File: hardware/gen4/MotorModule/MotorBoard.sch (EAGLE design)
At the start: 65 parts, among them IC1 XMEGA16A4A, M1O1 TEST_PT, M1O2 TEST_PT, M1O3 TEST_PT

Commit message: changes to motor and main board
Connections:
- net 12V: now also JP3.5, JP3.6
- net 12VGND: now also JP3.35, JP3.36
- net GND: now also JP3.33; no longer JP3.36
- net N$3: now also JP3.27; no longer JP3.31
- net N$34: now also JP3.31; no longer JP3.35
- net N$4: now also JP3.29; no longer JP3.33
- net N$45: now also JP3.25; no longer JP3.29
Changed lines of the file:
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@@
 <instance part="S2" gate="S" x="12.7" y="182.88"/>
 <instance part="GND10" gate="1" x="215.9" y="55.88" rot="R270"/>
-<instance part="GND14" gate="1" x="256.54" y="35.56"/>
+<instance part="GND14" gate="1" x="254" y="35.56"/>
 <instance part="U$1" gate="G$1" x="86.36" y="86.36" rot="R270"/>
 <instance part="C3" gate="G$1" x="111.76" y="132.08" rot="R180"/>
@@
 <pinref part="U$5" gate="G$1" pin="GND"/>
 <wire x1="215.9" y1="152.4" x2="215.9" y2="149.86" width="0.1524" layer="91"/>
-<label x="243.84" y="30.48" size="1.778" layer="95"/>
+<label x="243.84" y="33.02" size="1.778" layer="95"/>
 <pinref part="GND5" gate="1" pin="GND"/>
 </segment>
@@
 <segment>
 <pinref part="GND14" gate="1" pin="GND"/>
-<wire x1="256.54" y1="38.1" x2="241.3" y2="38.1" width="0.1524" layer="91"/>
+<wire x1="254" y1="38.1" x2="241.3" y2="38.1" width="0.1524" layer="91"/>
 <pinref part="JP3" gate="G$1" pin="30"/>
 <junction x="241.3" y="38.1"/>
@@
 </segment>
 <segment>
-<wire x1="241.3" y1="30.48" x2="243.84" y2="30.48" width="0.1524" layer="91"/>
-<wire x1="241.3" y1="30.48" x2="241.3" y2="33.02" width="0.1524" layer="91"/>
 <pinref part="JP3" gate="G$1" pin="34"/>
-<pinref part="JP3" gate="G$1" pin="36"/>
-<junction x="241.3" y="30.48"/>
+<wire x1="243.84" y1="33.02" x2="241.3" y2="33.02" width="0.1524" layer="91"/>
+<pinref part="JP3" gate="G$1" pin="33"/>
+<wire x1="241.3" y1="33.02" x2="226.06" y2="33.02" width="0.1524" layer="91"/>
 </segment>
 <segment>
@@
 <pinref part="R3" gate="G$1" pin="2"/>
 <wire x1="213.36" y1="20.32" x2="215.9" y2="20.32" width="0.1524" layer="91"/>
-<wire x1="215.9" y1="20.32" x2="215.9" y2="27.94" width="0.1524" layer="91"/>
-<wire x1="215.9" y1="27.94" x2="223.52" y2="35.56" width="0.1524" layer="91"/>
-<wire x1="223.52" y1="35.56" x2="226.06" y2="35.56" width="0.1524" layer="91"/>
-<pinref part="JP3" gate="G$1" pin="31"/>
+<wire x1="215.9" y1="20.32" x2="215.9" y2="30.48" width="0.1524" layer="91"/>
+<pinref part="JP3" gate="G$1" pin="27"/>
+<wire x1="215.9" y1="30.48" x2="226.06" y2="40.64" width="0.1524" layer="91"/>
 </segment>
 </net>
@@
 <segment>
 <pinref part="R4" gate="G$1" pin="2"/>
-<wire x1="218.44" y1="15.24" x2="218.44" y2="27.94" width="0.1524" layer="91"/>
-<wire x1="218.44" y1="27.94" x2="223.52" y2="33.02" width="0.1524" layer="91"/>
-<wire x1="223.52" y1="33.02" x2="226.06" y2="33.02" width="0.1524" layer="91"/>
-<pinref part="JP3" gate="G$1" pin="33"/>
+<wire x1="218.44" y1="15.24" x2="218.44" y2="30.48" width="0.1524" layer="91"/>
+<pinref part="JP3" gate="G$1" pin="29"/>
+<wire x1="226.06" y1="38.1" x2="218.44" y2="30.48" width="0.1524" layer="91"/>
 </segment>
 </net>
@@
 <junction x="226.06" y="73.66"/>
 <pinref part="JP3" gate="G$1" pin="3"/>
+<pinref part="JP3" gate="G$1" pin="5"/>
+<wire x1="226.06" y1="71.12" x2="226.06" y2="68.58" width="0.1524" layer="91"/>
+<pinref part="JP3" gate="G$1" pin="6"/>
+<wire x1="241.3" y1="71.12" x2="241.3" y2="68.58" width="0.1524" layer="91"/>
+<junction x="241.3" y="71.12"/>
+<junction x="226.06" y="71.12"/>
+<junction x="226.06" y="68.58"/>
+<junction x="241.3" y="68.58"/>
 </segment>
 <segment>
@@
 <wire x1="241.3" y1="25.4" x2="241.3" y2="27.94" width="0.1524" layer="91"/>
 <junction x="241.3" y="25.4"/>
+<pinref part="JP3" gate="G$1" pin="35"/>
+<wire x1="226.06" y1="27.94" x2="226.06" y2="30.48" width="0.1524" layer="91"/>
+<pinref part="JP3" gate="G$1" pin="36"/>
+<wire x1="241.3" y1="27.94" x2="241.3" y2="30.48" width="0.1524" layer="91"/>
+<junction x="226.06" y="27.94"/>
+<junction x="226.06" y="30.48"/>
+<junction x="241.3" y="30.48"/>
+<junction x="241.3" y="27.94"/>
 </segment>
 <segment>
@@
 <segment>
 <pinref part="R2" gate="G$1" pin="2"/>
-<wire x1="213.36" y1="25.4" x2="213.36" y2="27.94" width="0.1524" layer="91"/>
-<wire x1="213.36" y1="27.94" x2="223.52" y2="38.1" width="0.1524" layer="91"/>
-<wire x1="223.52" y1="38.1" x2="226.06" y2="38.1" width="0.1524" layer="91"/>
-<pinref part="JP3" gate="G$1" pin="29"/>
+<pinref part="JP3" gate="G$1" pin="25"/>
+<wire x1="226.06" y1="43.18" x2="213.36" y2="30.48" width="0.1524" layer="91"/>
+<wire x1="213.36" y1="30.48" x2="213.36" y2="25.4" width="0.1524" layer="91"/>
 </segment>
 </net>
@@
 <segment>
 <pinref part="R15" gate="G$1" pin="2"/>
-<wire x1="223.52" y1="10.16" x2="223.52" y2="30.48" width="0.1524" layer="91"/>
-<wire x1="223.52" y1="30.48" x2="226.06" y2="30.48" width="0.1524" layer="91"/>
-<pinref part="JP3" gate="G$1" pin="35"/>
-</segment>
-</net>
+<wire x1="223.52" y1="10.16" x2="223.52" y2="33.02" width="0.1524" layer="91"/>
+<pinref part="JP3" gate="G$1" pin="31"/>
+<wire x1="223.52" y1="33.02" x2="226.06" y2="35.56" width="0.1524" layer="91"/>
+</segment>
+</net>

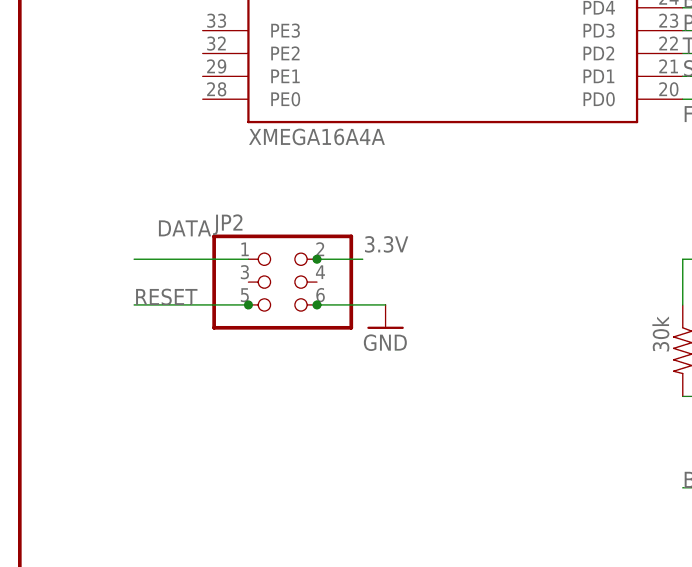
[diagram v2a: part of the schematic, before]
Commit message: motor board push button fix
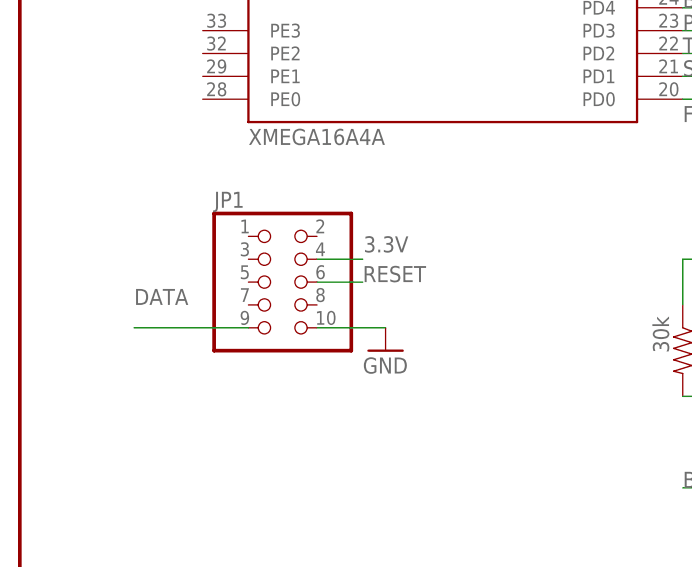
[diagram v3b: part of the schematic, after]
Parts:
- removed JP2: (no value), pinhead:PINHD-2X3
- added JP1: (no value), pinhead:PINHD-2X5
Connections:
- net 3.3V: now also JP1.4; no longer JP2.2
- net DATA: now also JP1.9; no longer JP2.1
- net GND: now also JP1.10; no longer JP2.6
- net RESET: now also JP1.6; no longer JP2.5
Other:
- note removed: "RESET"
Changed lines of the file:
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@@
 <part name="GND15" library="SparkFun-Aesthetics" deviceset="GND" device=""/>
 <part name="GND16" library="SparkFun-Aesthetics" deviceset="GND" device=""/>
-<part name="JP2" library="pinhead" deviceset="PINHD-2X3" device=""/>
 <part name="R18" library="resistor" deviceset="R-US_" device="R2512" value="0.05"/>
+<part name="JP1" library="pinhead" deviceset="PINHD-2X5" device=""/>
 </parts>
 <sheets>
@@
 <text x="73.66" y="88.9" size="1.778" layer="95">FAULTN
 </text>
-<text x="12.7" y="68.58" size="1.778" layer="95">RESET</text>
 <text x="78.74" y="25.4" size="1.778" layer="95">ENABLE</text>
 <text x="73.66" y="106.68" size="1.778" layer="95">ENABLE</text>
@@
 <instance part="R11" gate="G$1" x="91.44" y="25.4" rot="R180"/>
 <instance part="R15" gate="G$1" x="218.44" y="10.16"/>
-<instance part="GND1" gate="1" x="40.64" y="66.04"/>
+<instance part="GND1" gate="1" x="40.64" y="63.5"/>
 <instance part="IC2" gate="G$1" x="127" y="132.08"/>
 <instance part="GND4" gate="1" x="127" y="124.46"/>
@@
 <instance part="GND15" gate="1" x="111.76" y="124.46"/>
 <instance part="GND16" gate="1" x="142.24" y="124.46"/>
-<instance part="JP2" gate="A" x="27.94" y="71.12"/>
 <instance part="R18" gate="G$1" x="149.86" y="7.62" rot="R90"/>
+<instance part="JP1" gate="A" x="27.94" y="71.12"/>
 </instances>
 <busses>
@@
 </segment>
 <segment>
-<wire x1="33.02" y1="68.58" x2="40.64" y2="68.58" width="0.1524" layer="91"/>
+<wire x1="33.02" y1="66.04" x2="40.64" y2="66.04" width="0.1524" layer="91"/>
 <pinref part="GND1" gate="1" pin="GND"/>
-<pinref part="JP2" gate="A" pin="6"/>
-<junction x="33.02" y="68.58"/>
+<pinref part="JP1" gate="A" pin="10"/>
 </segment>
 <segment>
@@
 </segment>
 <segment>
-<wire x1="12.7" y1="68.58" x2="25.4" y2="68.58" width="0.1524" layer="91"/>
-<pinref part="JP2" gate="A" pin="5"/>
-<junction x="25.4" y="68.58"/>
+<wire x1="33.02" y1="71.12" x2="38.1" y2="71.12" width="0.1524" layer="91"/>
+<label x="38.1" y="71.12" size="1.778" layer="95"/>
+<pinref part="JP1" gate="A" pin="6"/>
 </segment>
 </net>
@@
 <segment>
 <wire x1="33.02" y1="73.66" x2="38.1" y2="73.66" width="0.1524" layer="91"/>
-<pinref part="JP2" gate="A" pin="2"/>
-<junction x="33.02" y="73.66"/>
+<pinref part="JP1" gate="A" pin="4"/>
 </segment>
 <segment>
@@
 </segment>
 <segment>
-<pinref part="JP2" gate="A" pin="1"/>
-<wire x1="25.4" y1="73.66" x2="12.7" y2="73.66" width="0.1524" layer="91"/>
-<label x="15.24" y="76.2" size="1.778" layer="95"/>
-</segment>
-</net>
+<wire x1="25.4" y1="66.04" x2="12.7" y2="66.04" width="0.1524" layer="91"/>
+<label x="12.7" y="68.58" size="1.778" layer="95"/>
+<pinref part="JP1" gate="A" pin="9"/>
+</segment>
+</net>

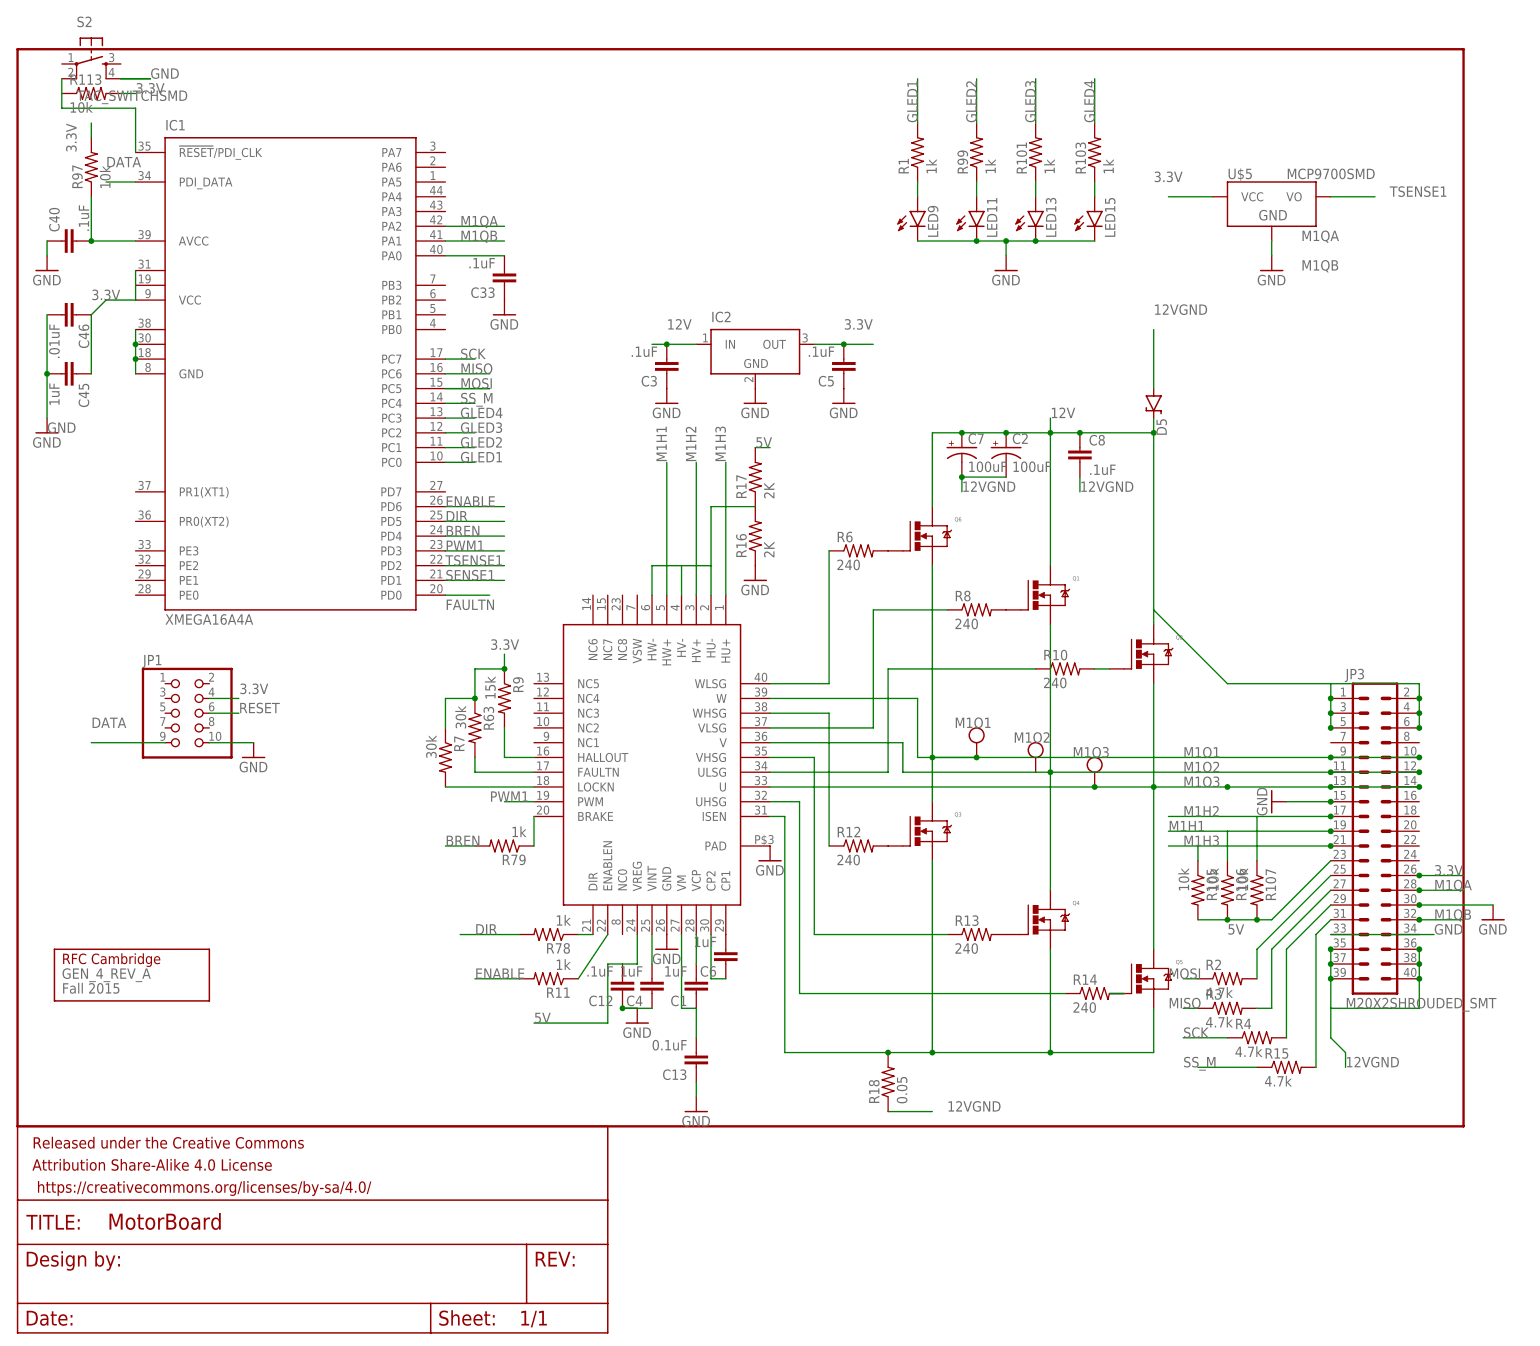
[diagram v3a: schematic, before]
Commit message: fixed ten thousand net issues on motorboard
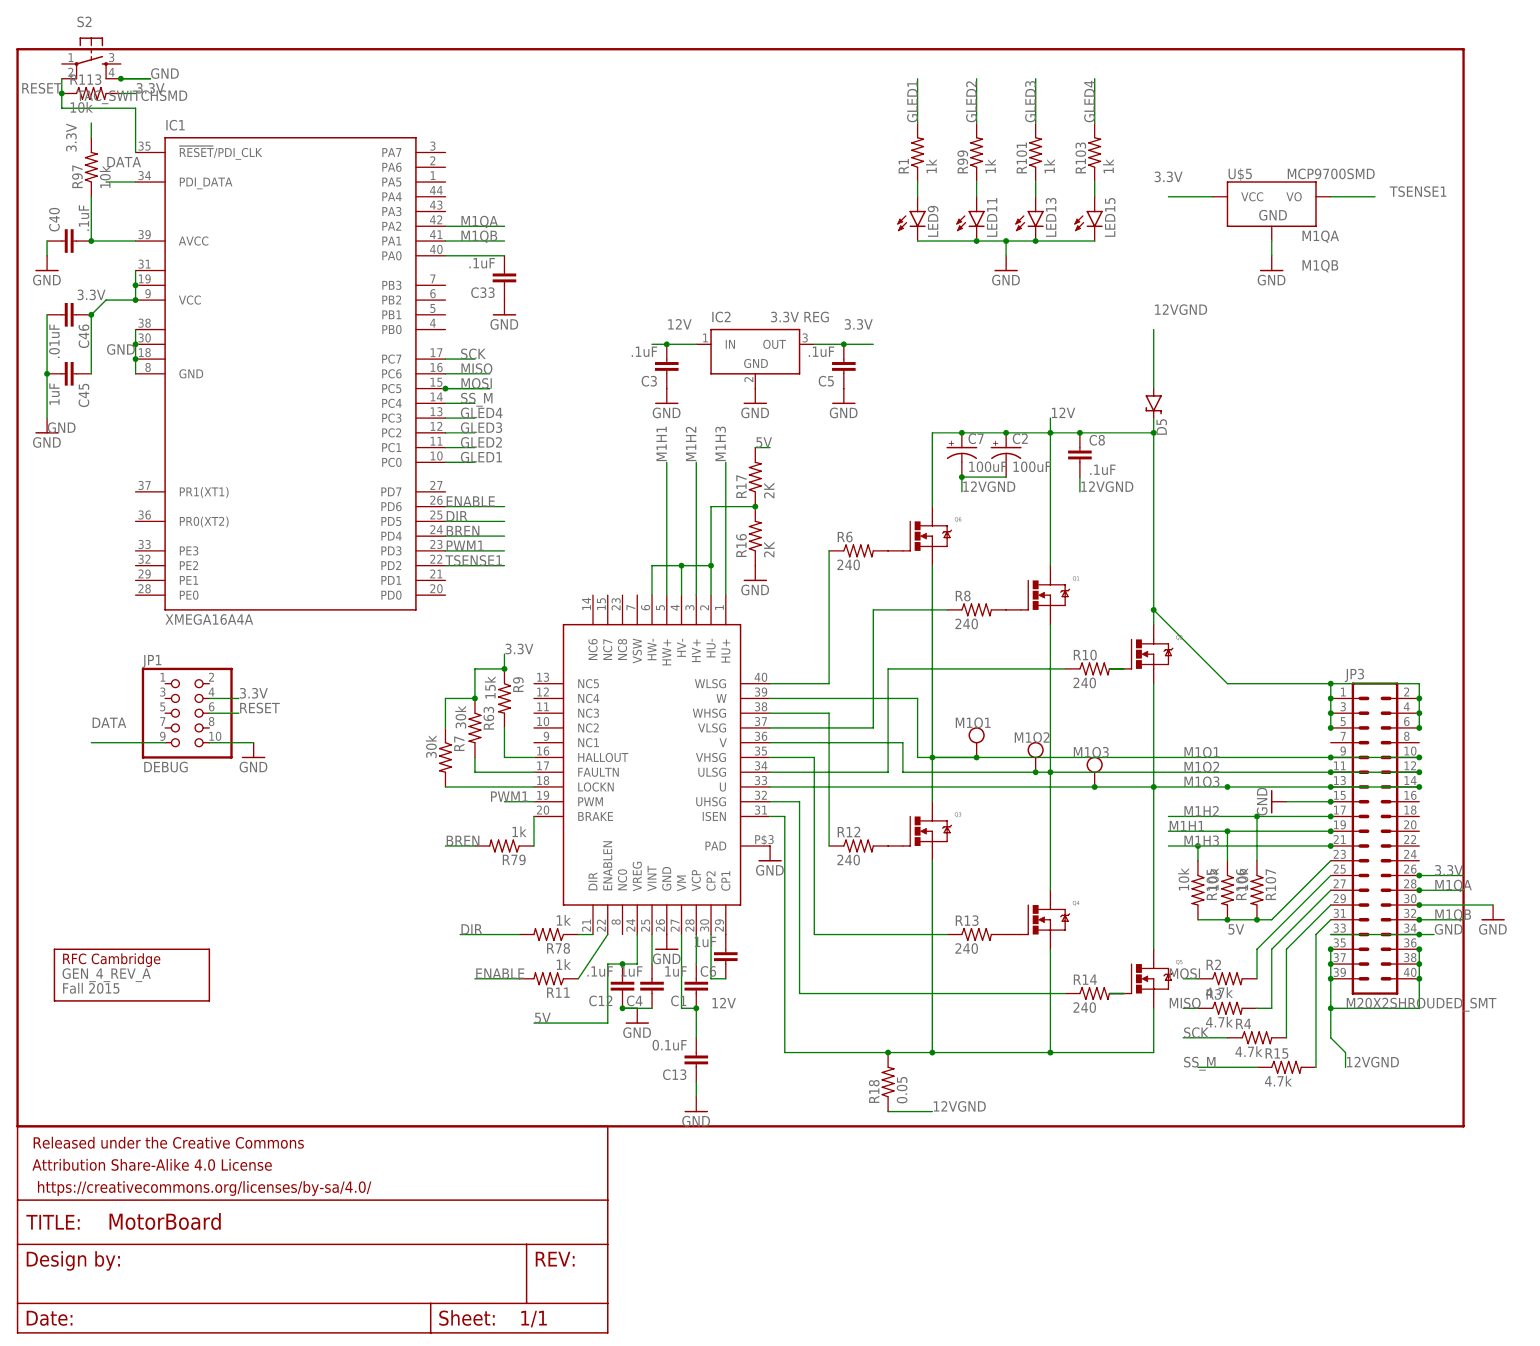
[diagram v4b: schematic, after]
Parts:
- IC2: value (none) -> 3.3V REG
- JP1: value (none) -> DEBUG
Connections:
- removed net FAULT1: IC1.PD0
- removed net SENSE1: IC1.PD1
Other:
- note removed: "5V"
- note removed: "DIR"
- note removed: "ENABLE"
- note removed: "FAULTN"
- note removed: "SENSE1"
- note removed: "TSENSE1"
- moved on the sheet: R10

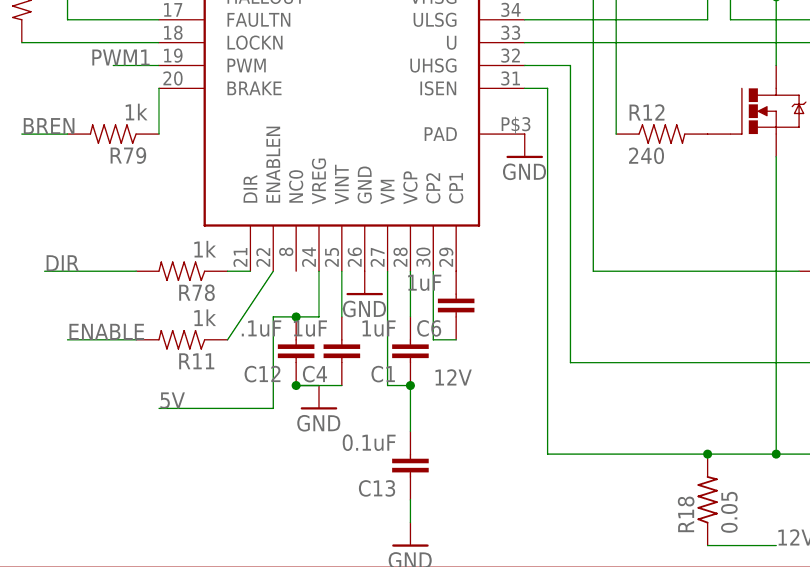
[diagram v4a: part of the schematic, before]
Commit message: changed cap value on motorboard (CP1 and CP2)
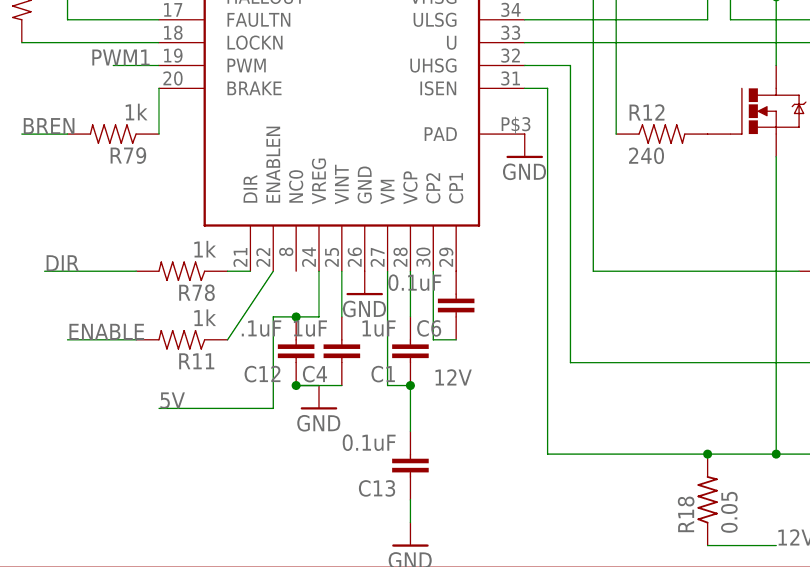
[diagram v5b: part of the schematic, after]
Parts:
- C6: value 1uF -> 0.1uF
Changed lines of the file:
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@@
 <part name="R4" library="SparkFun-Passives" deviceset="RESISTOR" device="0805-RES" value="4.7k"/>
 <part name="C4" library="SparkFun-Passives" deviceset="CAP" device="0805" value="1uF"/>
-<part name="C6" library="SparkFun-Passives" deviceset="CAP" device="0805" value="1uF"/>
+<part name="C6" library="SparkFun-Passives" deviceset="CAP" device="0805" value="0.1uF"/>
 <part name="GND2" library="SparkFun-Aesthetics" deviceset="GND" device=""/>
 <part name="GND3" library="SparkFun-Aesthetics" deviceset="GND" device=""/>
